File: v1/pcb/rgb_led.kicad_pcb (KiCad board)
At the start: 2 copper layers, 62.7 x 45.2 mm, 9 parts, among them P1 CONN_2, P2 CONN_4, SW1 SWITCH_INV

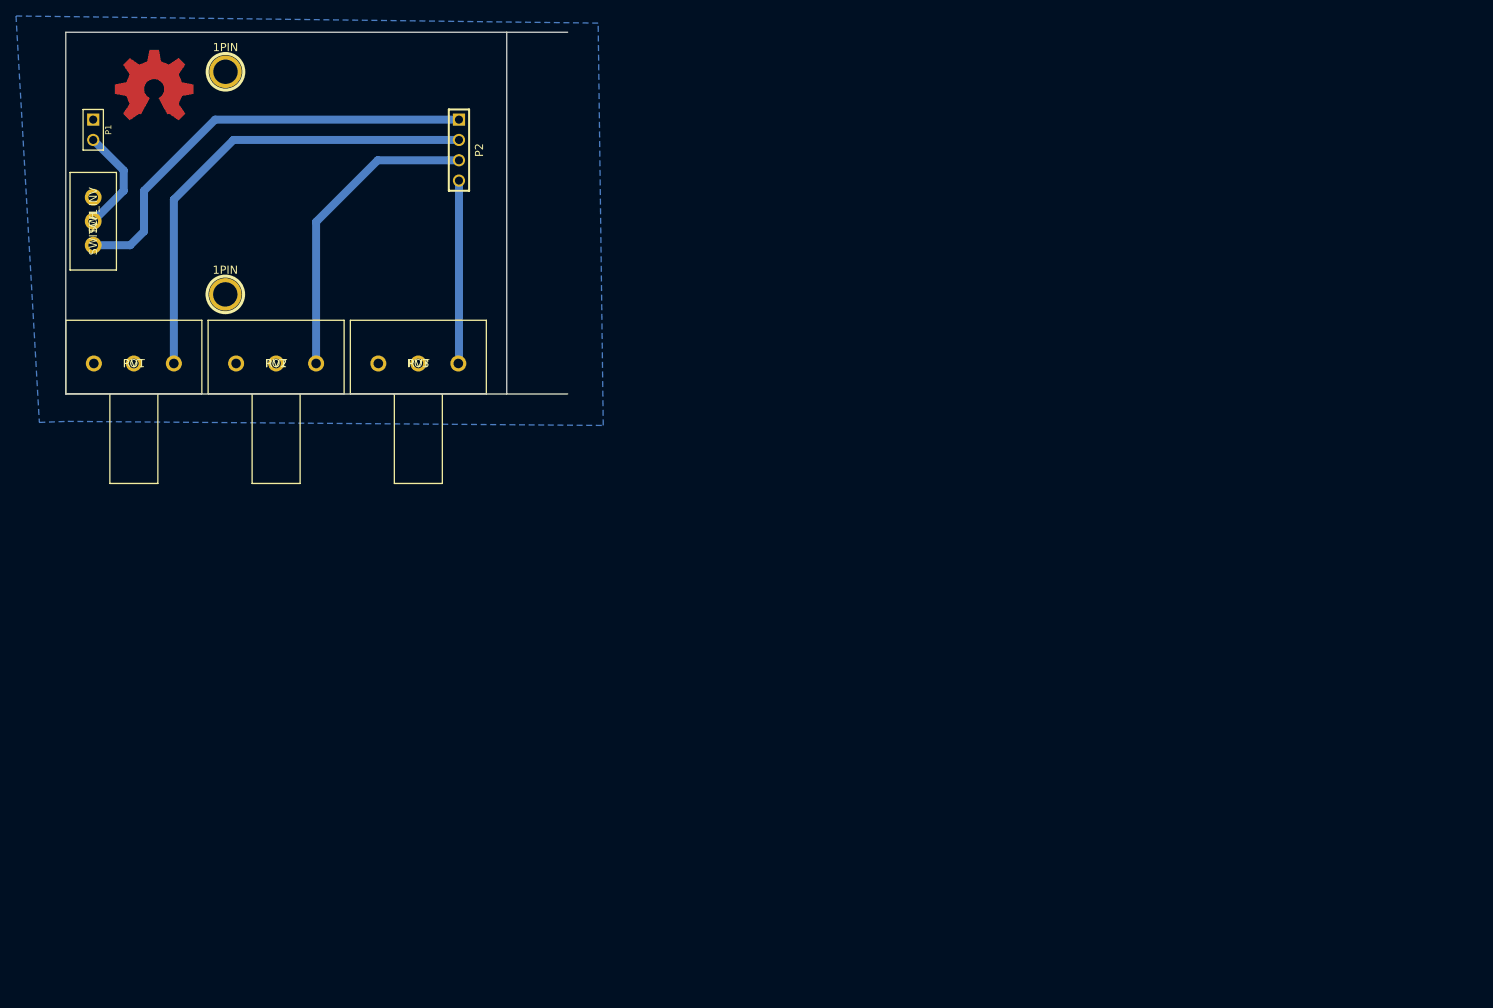
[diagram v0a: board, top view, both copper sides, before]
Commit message: Changed footprint page size to A4
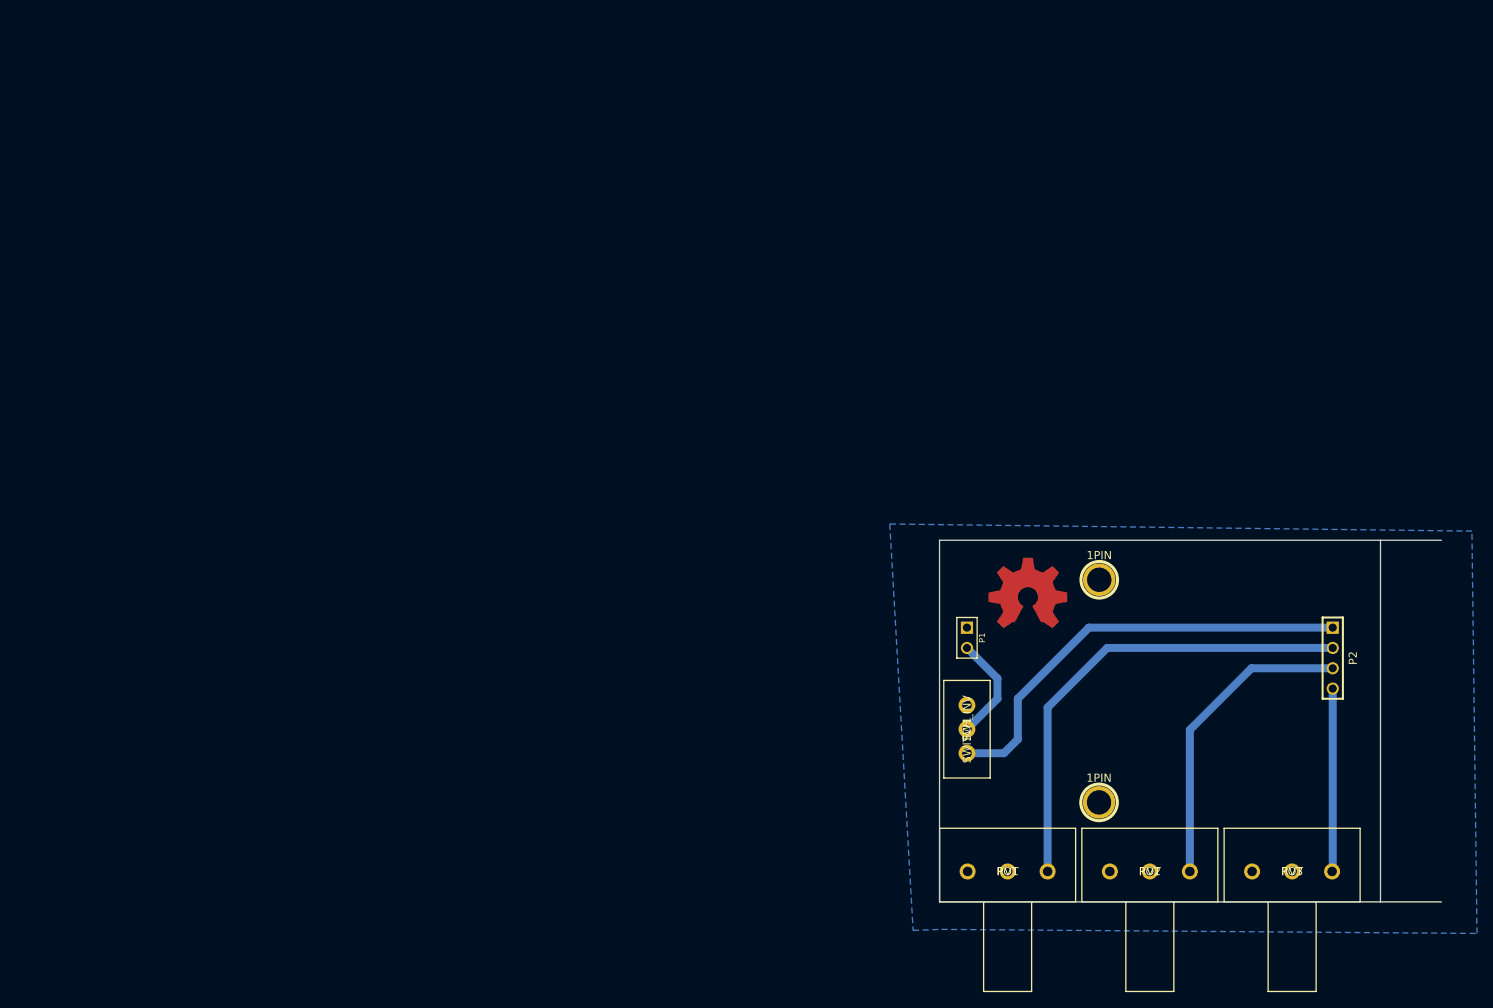
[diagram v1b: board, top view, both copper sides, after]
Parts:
- moved P1 126.3 mm to (132.1, 87.6)
- moved P2 126.3 mm to (177.8, 90.2)
- moved SW1 126.3 mm to (132.1, 99.1)
- moved 1PIN 126.3 mm to (148.6, 80.4)
- moved 1PIN 126.3 mm to (148.6, 108.2)
- moved RV1 126.3 mm to (137.2, 116.8)
- moved RV2 126.3 mm to (154.9, 116.8)
- moved RV3 126.3 mm to (172.7, 116.8)
- moved OSHW_LOGO 126.3 mm to (139.7, 82.5)
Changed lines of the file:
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@@
     (nets 7)
   )
-  (page A3)
+  (page A4)
+  (title_block
+    (title "RGB LED")
+    (rev 1.1)
+    (company Coredump)
+  )
   (layers
     (15 F.Cu signal)
@@
   )
   (module POT_3 (layer F.Cu)
-    (at 45.72 53.34)
+    (at 154.94 116.84)
     (fp_text reference RV2 (at 0 0) (layer F.SilkS)
       (effects (font (size 1 1) (thickness 0.15)))
@@
   )
   (module POT_3 (layer F.Cu)
-    (at 63.5 53.34)
+    (at 172.72 116.84)
     (fp_text reference RV3 (at 0 0) (layer F.SilkS)
       (effects (font (size 1 1) (thickness 0.15)))
@@
   )
   (module POT_3 (layer F.Cu)
-    (at 27.94 53.34)
+    (at 137.16 116.84)
     (fp_text reference RV1 (at 0 0) (layer F.SilkS)
       (effects (font (size 1 1) (thickness 0.15)))
@@
   )
   (module PIN_ARRAY_4x1 (layer F.Cu)
-    (at 68.58 26.67 270)
+    (at 177.8 90.17 270)
     (descr "Double rangee de contacts 2 x 5 pins")
     (tags CONN)
@@
   )
   (module PIN_ARRAY_2X1 (layer F.Cu)
-    (at 22.86 24.13 270)
+    (at 132.08 87.63 270)
     (descr "Connecteurs 2 pins")
     (tags "CONN DEV")
@@
   )
   (module 1pin (layer F.Cu)
-    (at 39.3954 16.8783)
+    (at 148.6154 80.3783)
     (descr "module 1 pin (ou trou mecanique de percage)")
     (tags DEV)
@@
   )
   (module 1pin (layer F.Cu)
-    (at 39.37 44.704)
+    (at 148.59 108.204)
     (descr "module 1 pin (ou trou mecanique de percage)")
     (tags DEV)
@@
   )
   (module Switch_SS-12F46 (layer F.Cu)
-    (at 22.86 35.56 90)
+    (at 132.08 99.06 90)
     (fp_text reference SW1 (at 0 0 90) (layer F.SilkS)
       (effects (font (size 1 1) (thickness 0.15)))
@@
   )
   (module OSHW_COPPER_10MM (layer F.Cu)
-    (at 30.48 19.05)
+    (at 139.7 82.55)
     (fp_text reference OSHW_LOGO (at 0 6.35) (layer F.SilkS) hide
       (effects (font (size 1.524 1.524) (thickness 0.3048)))
@@
     )
   )
-  (gr_text B (at 63.5 45.72) (layer B.Mask)
+  (gr_text B (at 172.72 109.22) (layer B.Mask)
     (effects (font (size 1.5 1.5) (thickness 0.3)) (justify mirror))
   )
-  (gr_text R (at 45.72 45.72) (layer B.Mask)
+  (gr_text R (at 154.94 109.22) (layer B.Mask)
     (effects (font (size 1.5 1.5) (thickness 0.3)) (justify mirror))
   )
-  (gr_text G (at 27.94 45.72) (layer B.Mask)
+  (gr_text G (at 137.16 109.22) (layer B.Mask)
     (effects (font (size 1.5 1.5) (thickness 0.3)) (justify mirror))
   )
-  (gr_text "coredump\nRGB LED V1.1 2015" (at 58.42 15.24) (layer B.Mask)
+  (gr_text "coredump\nRGB LED V1.1 2015" (at 167.64 78.74) (layer B.Mask)
     (effects (font (size 2 2) (thickness 0.3)) (justify mirror))
   )
-  (gr_line (start 19.431 57.15) (end 82.169 57.15) (angle 90) (layer Edge.Cuts) (width 0.1))
-  (gr_line (start 19.431 11.938) (end 19.431 57.15) (angle 90) (layer Edge.Cuts) (width 0.1))
-  (gr_line (start 82.169 11.938) (end 19.431 11.938) (angle 90) (layer Edge.Cuts) (width 0.1))
-  (gr_line (start 74.549 57.15) (end 74.549 11.938) (angle 90) (layer Edge.Cuts) (width 0.1))
-  (segment (start 68.58 53.26) (end 68.5 53.34) (width 1) (layer B.Cu) (net 2))
-  (segment (start 68.58 30.48) (end 68.58 53.26) (width 1) (layer B.Cu) (net 2))
-  (segment (start 50.72 53.34) (end 50.72 35.64) (width 1) (layer B.Cu) (net 3))
-  (segment (start 50.72 35.64) (end 58.42 27.94) (width 1) (layer B.Cu) (net 3))
-  (segment (start 58.42 27.94) (end 68.58 27.94) (width 1) (layer B.Cu) (net 3))
-  (segment (start 32.94 53.34) (end 32.94 32.846) (width 1) (layer B.Cu) (net 4))
-  (segment (start 40.386 25.4) (end 68.58 25.4) (width 1) (layer B.Cu) (net 4))
-  (segment (start 32.94 32.846) (end 40.386 25.4) (width 1) (layer B.Cu) (net 4))
-  (segment (start 68.58 22.86) (end 38.1 22.86) (width 1) (layer B.Cu) (net 5))
-  (segment (start 27.48 38.56) (end 22.86 38.56) (width 1) (layer B.Cu) (net 5))
-  (segment (start 29.21 36.83) (end 27.48 38.56) (width 1) (layer B.Cu) (net 5))
-  (segment (start 29.21 31.75) (end 29.21 36.83) (width 1) (layer B.Cu) (net 5))
-  (segment (start 38.1 22.86) (end 29.21 31.75) (width 1) (layer B.Cu) (net 5))
-  (segment (start 22.86 25.4) (end 26.67 29.21) (width 1) (layer B.Cu) (net 6))
-  (segment (start 26.67 31.75) (end 22.86 35.56) (width 1) (layer B.Cu) (net 6))
-  (segment (start 26.67 29.21) (end 26.67 31.75) (width 1) (layer B.Cu) (net 6))
+  (gr_line (start 128.651 120.65) (end 191.389 120.65) (angle 90) (layer Edge.Cuts) (width 0.1))
+  (gr_line (start 128.651 75.438) (end 128.651 120.65) (angle 90) (layer Edge.Cuts) (width 0.1))
+  (gr_line (start 191.389 75.438) (end 128.651 75.438) (angle 90) (layer Edge.Cuts) (width 0.1))
+  (gr_line (start 183.769 120.65) (end 183.769 75.438) (angle 90) (layer Edge.Cuts) (width 0.1))
+  (segment (start 177.8 116.76) (end 177.72 116.84) (width 1) (layer B.Cu) (net 2))
+  (segment (start 177.8 93.98) (end 177.8 116.76) (width 1) (layer B.Cu) (net 2))
+  (segment (start 159.94 116.84) (end 159.94 99.14) (width 1) (layer B.Cu) (net 3))
+  (segment (start 159.94 99.14) (end 167.64 91.44) (width 1) (layer B.Cu) (net 3))
+  (segment (start 167.64 91.44) (end 177.8 91.44) (width 1) (layer B.Cu) (net 3))
+  (segment (start 142.16 116.84) (end 142.16 96.346) (width 1) (layer B.Cu) (net 4))
+  (segment (start 149.606 88.9) (end 177.8 88.9) (width 1) (layer B.Cu) (net 4))
+  (segment (start 142.16 96.346) (end 149.606 88.9) (width 1) (layer B.Cu) (net 4))
+  (segment (start 177.8 86.36) (end 147.32 86.36) (width 1) (layer B.Cu) (net 5))
+  (segment (start 136.7 102.06) (end 132.08 102.06) (width 1) (layer B.Cu) (net 5))
+  (segment (start 138.43 100.33) (end 136.7 102.06) (width 1) (layer B.Cu) (net 5))
+  (segment (start 138.43 95.25) (end 138.43 100.33) (width 1) (layer B.Cu) (net 5))
+  (segment (start 147.32 86.36) (end 138.43 95.25) (width 1) (layer B.Cu) (net 5))
+  (segment (start 132.08 88.9) (end 135.89 92.71) (width 1) (layer B.Cu) (net 6))
+  (segment (start 135.89 95.25) (end 132.08 99.06) (width 1) (layer B.Cu) (net 6))
+  (segment (start 135.89 92.71) (end 135.89 95.25) (width 1) (layer B.Cu) (net 6))
   (zone (net 1) (net_name GND) (layer B.Cu) (hatch edge 0.508)
     (connect_pads (clearance 0.508))
@@
     (polygon
       (pts
-        (xy 86.614 61.087) (xy 85.979 10.795) (xy 13.208 9.906) (xy 16.129 60.706) (xy 19.685 60.579)
+        (xy 195.834 124.587) (xy 195.199 74.295) (xy 122.428 73.406) (xy 125.349 124.206) (xy 128.905 124.079)
       )
     )

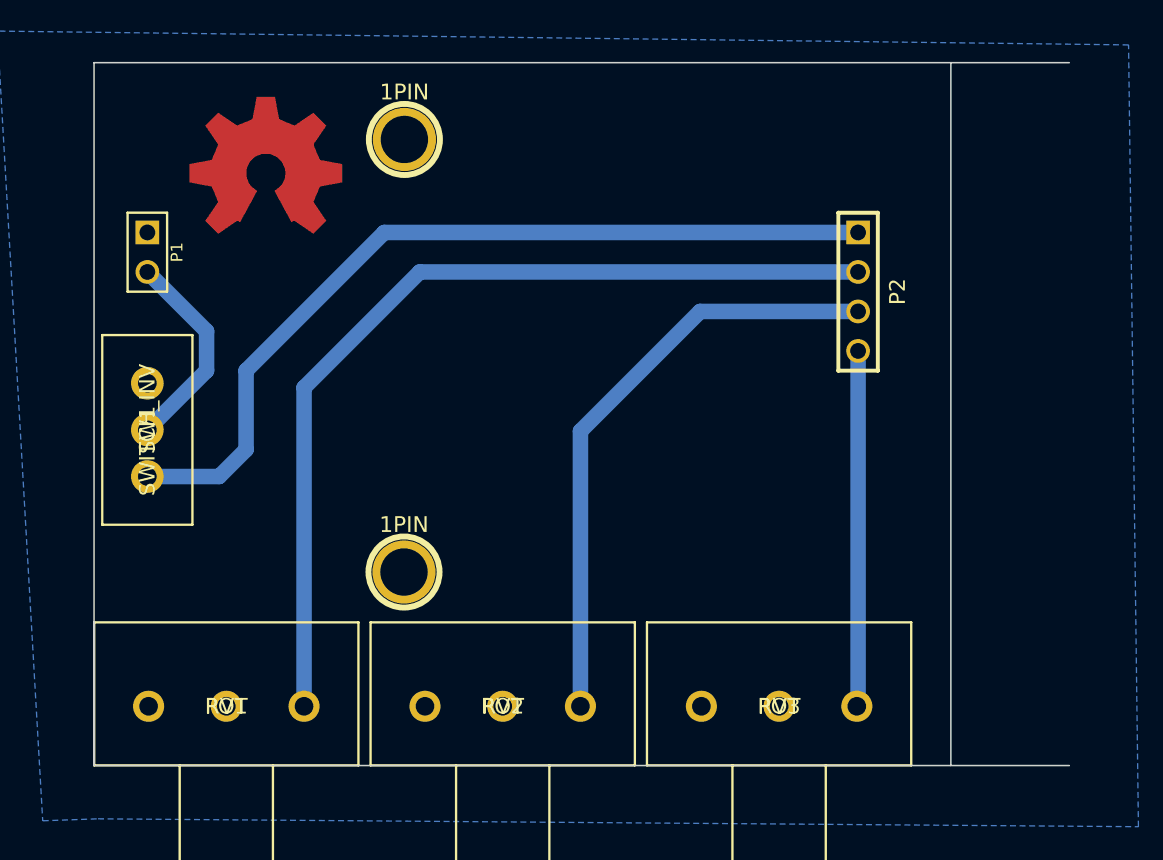
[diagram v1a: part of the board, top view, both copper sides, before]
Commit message: Actually fixed edge cuts
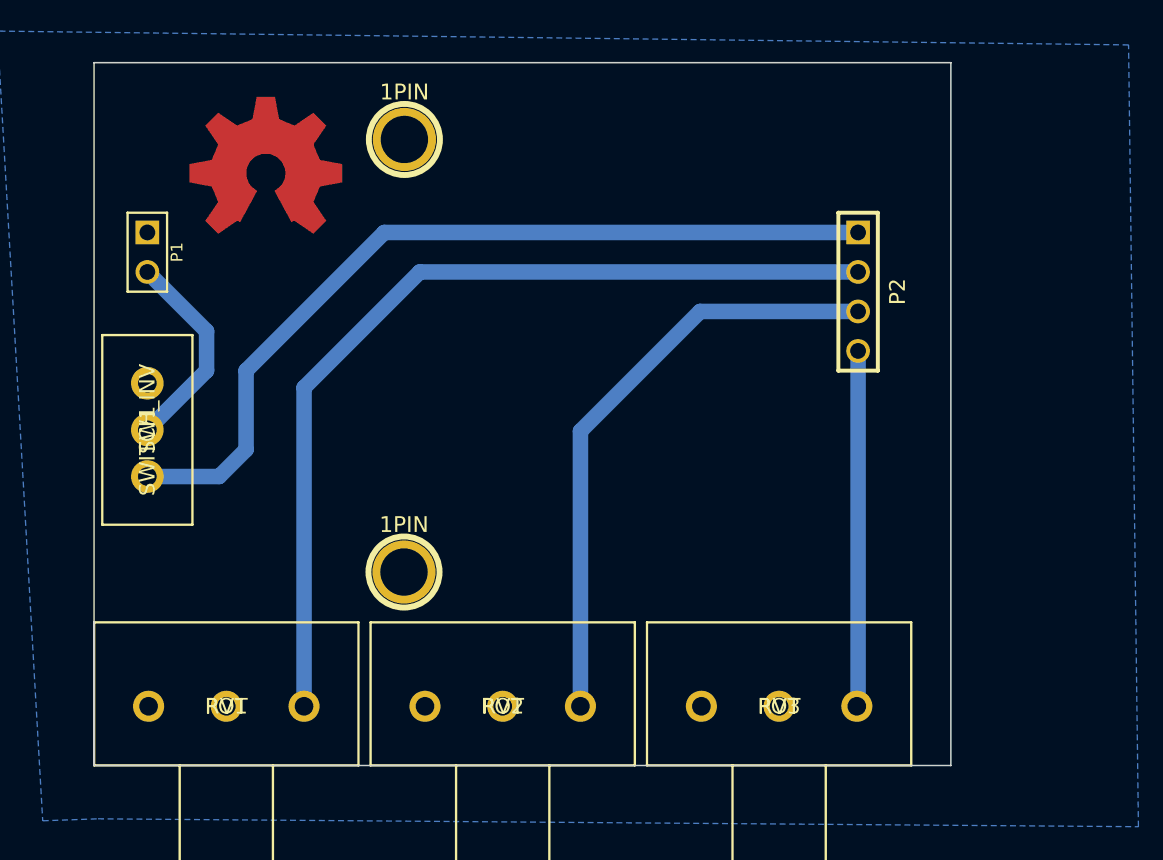
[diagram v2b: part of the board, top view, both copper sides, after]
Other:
- board size 62.7 x 45.2 mm -> 55.1 x 45.2 mm
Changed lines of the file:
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@@
     )
   )
+  (gr_line (start 183.769 75.438) (end 128.651 75.438) (angle 90) (layer Edge.Cuts) (width 0.1))
   (gr_text B (at 172.72 109.22) (layer B.Mask)
     (effects (font (size 1.5 1.5) (thickness 0.3)) (justify mirror))
@@
     (effects (font (size 2 2) (thickness 0.3)) (justify mirror))
   )
-  (gr_line (start 128.651 120.65) (end 191.389 120.65) (angle 90) (layer Edge.Cuts) (width 0.1))
+  (gr_line (start 128.651 120.65) (end 183.769 120.65) (angle 90) (layer Edge.Cuts) (width 0.1))
   (gr_line (start 128.651 75.438) (end 128.651 120.65) (angle 90) (layer Edge.Cuts) (width 0.1))
-  (gr_line (start 191.389 75.438) (end 128.651 75.438) (angle 90) (layer Edge.Cuts) (width 0.1))
   (gr_line (start 183.769 120.65) (end 183.769 75.438) (angle 90) (layer Edge.Cuts) (width 0.1))
   (segment (start 177.8 116.76) (end 177.72 116.84) (width 1) (layer B.Cu) (net 2))
